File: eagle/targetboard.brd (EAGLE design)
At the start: 99.4 x 49.6 mm, 80 parts, among them CN1 DIP-BLACK-MALE-HEADER-VERT(3P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, IC1 MCP2551, IC2 LPC1768 or LPC1768, IC3 PMIC-CJT1117-3.3(SOT223), IC4 MCP2551, IC5 TB6612FNG, IC6 TB6612FNG, IC7 MAX232D, J1 DIP-BLACK-MALE-HEADER-VERT(8P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, J10 CAN1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

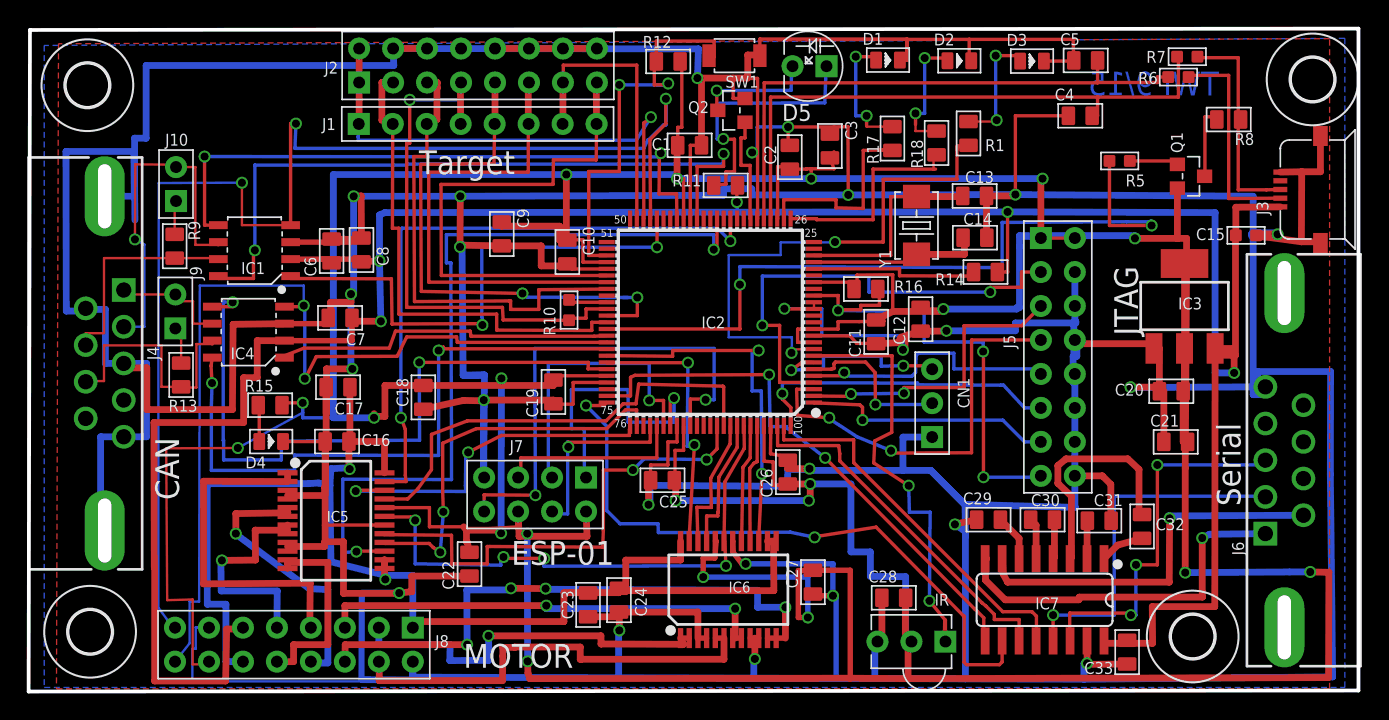
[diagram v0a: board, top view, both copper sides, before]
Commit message: Fix Board revision, CAN VCC and VSS mixed up
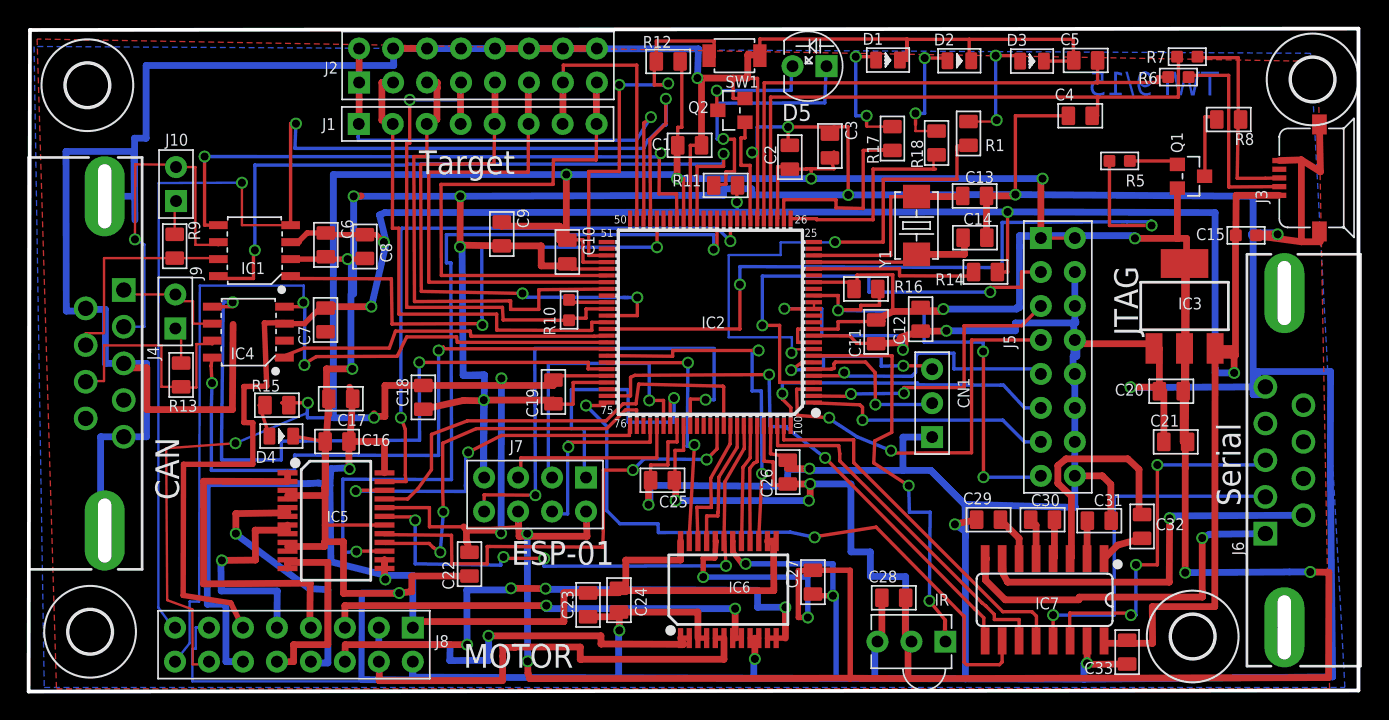
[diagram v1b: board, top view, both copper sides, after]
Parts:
- moved C7 1.10 mm to (22.4, 27.7), turned to 180 degrees
- moved C17 0.89 mm to (23.5, 21.8)
- moved J3 0.87 mm to (93.7, 38.4)
- moved D4 0.86 mm to (19.1, 19.1)
- moved C6 0.63 mm to (22.4, 33.4), turned to 0 degrees
- moved R15 0.51 mm to (18.7, 21.4)
- moved C8 0.36 mm to (25.3, 33.2)
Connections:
- net GND: now also C7.1, C8.1, IC1.2, IC4.2; no longer C7.2, C8.2, IC1.3, IC4.3
- net VCC: now also C7.2, C8.2, IC1.3, IC4.3; no longer C7.1, C8.1, IC1.2, IC4.2
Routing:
- net VCC: track 204.2 -> 191.9 mm
- net GND: track 835.9 -> 824.0 mm
- net CAN2_RX: track 70.5 -> 68.9 mm
- net DM: track 16.3 -> 15.3 mm
- net DP: track 16.3 -> 15.5 mm
